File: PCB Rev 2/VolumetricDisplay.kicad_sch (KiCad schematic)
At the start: 0 parts

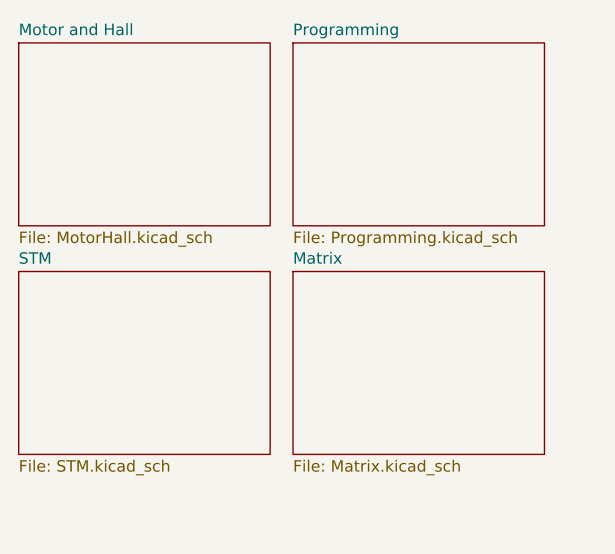
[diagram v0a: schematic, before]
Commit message: updated to RP2354 & misc cleanup
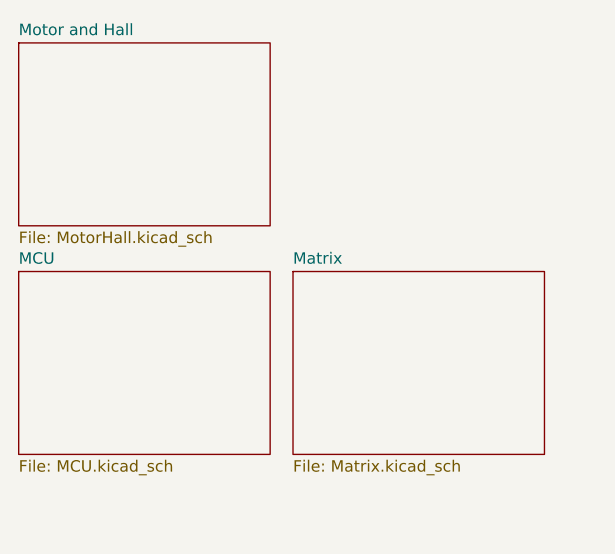
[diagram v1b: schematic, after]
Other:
- sheet STM renamed MCU
- removed sheet Programming
- sheet MCU: file STM.kicad_sch -> MCU.kicad_sch
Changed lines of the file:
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@@
-	)
-	(sheet
-		(at 151.13 69.85)
-		(size 27.94 20.32)
-		(exclude_from_sim no)
-		(in_bom yes)
-		(on_board yes)
-		(dnp no)
-		(fields_autoplaced yes)
-		(stroke
-			(width 0.1524)
-			(type solid)
-		)
-		(fill
-			(color 0 0 0 0)
-		)
-		(property "Sheetname" "Programming"
-			(at 151.13 69.1384 0)
-			(show_name no)
-			(do_not_autoplace no)
-			(effects
-				(font
-					(size 1.27 1.27)
-				)
-				(justify left bottom)
-			)
-		)
-		(property "Sheetfile" "Programming.kicad_sch"
-			(at 151.13 90.7546 0)
-			(show_name no)
-			(do_not_autoplace no)
-			(effects
-				(font
-					(size 1.27 1.27)
-				)
-				(justify left top)
-			)
-		)
-		(instances
-			(project "VolumetricDisplay"
-				(path "/7bd694af-37ad-47ba-90df-07da5b1590c2"
-					(page "3")
-				)
-			)
-		)
 	)
 	(sheet
@@
 			(color 0 0 0 0)
 		)
-		(property "Sheetname" "STM"
+		(property "Sheetname" "MCU"
 			(at 120.65 94.5384 0)
 			(show_name no)
@@
 			)
 		)
-		(property "Sheetfile" "STM.kicad_sch"
+		(property "Sheetfile" "MCU.kicad_sch"
 			(at 120.65 116.1546 0)
 			(show_name no)
